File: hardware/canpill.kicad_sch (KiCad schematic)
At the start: 57 parts, among them J1 TYPE-C-31-M-12, J2 5100TR, J3 5100TR, J4 1776112-4, J5 Conn_01x20_Pin, J6 Conn_01x16_Pin, J7 FTSH-105-01-L-DV-K, SW1 SW_SPDT, SW2 SW_Push, U1 STM32F103C8T6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

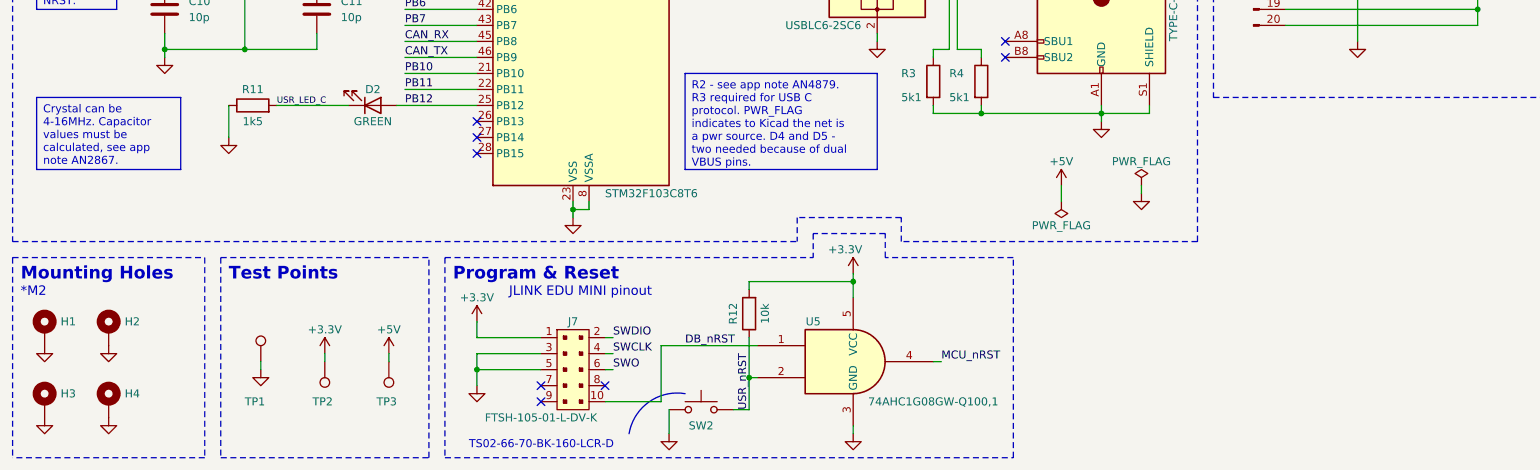
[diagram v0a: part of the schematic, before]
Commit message: (software:canpill_test) initial commit; (hardware) add pull-up on DB_nRST
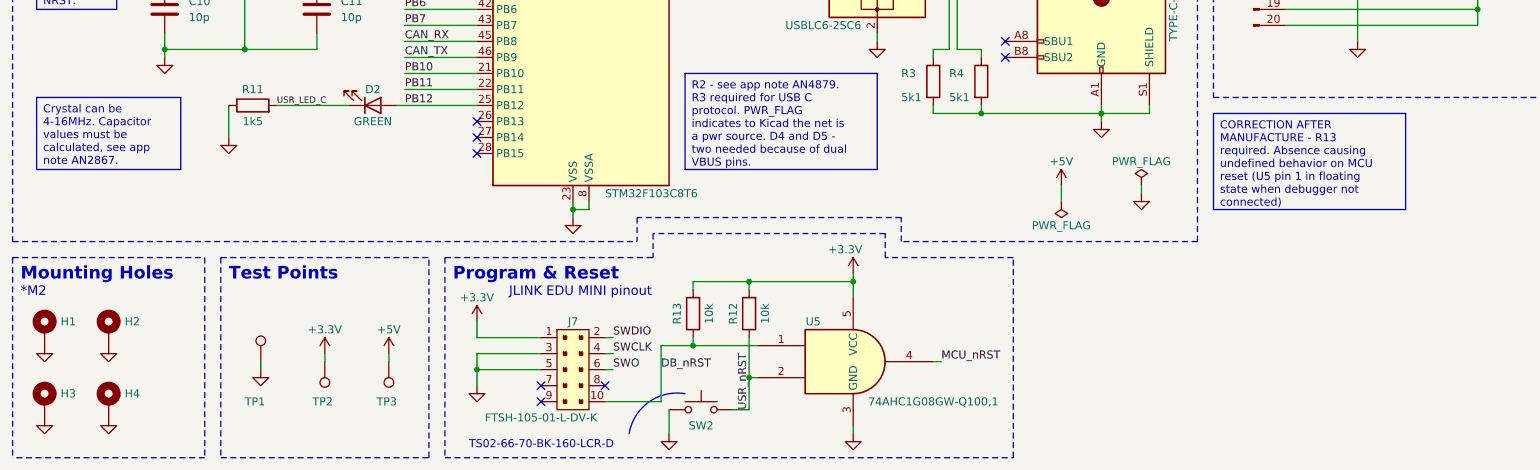
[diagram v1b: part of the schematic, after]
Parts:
- added R13: 10k, Resistor_SMD:R_0402_1005Metric, symbol Device:R
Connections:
- net +3.3V: now also R13.2
- net DB_nRST: now also R13.1
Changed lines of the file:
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@@
   (junction (at 148.59 167.64) (diameter 0) (color 0 0 0 0)
   )
+  (junction (at 123.19 177.8) (diameter 0) (color 0 0 0 0)
+  )
   (junction (at 182.88 24.13) (diameter 0) (color 0 0 0 0)
   )
@@
   )
   (junction (at 228.6 81.28) (diameter 0) (color 0 0 0 0)
+  )
+  (junction (at 132.08 167.64) (diameter 0) (color 0 0 0 0)
   )
   (junction (at 254 119.38) (diameter 0) (color 0 0 0 0)
@@
     (stroke (width 0) (type default))
   )
-  (wire (pts (xy 118.11 177.8) (xy 133.35 177.8))
-    (stroke (width 0) (type default))
-  )
   (wire (pts (xy 77.47 134.62) (xy 88.9 134.62))
     (stroke (width 0) (type default))
@@
     (stroke (width 0) (type dash))
   )
-  (polyline (pts (xy 15.24 161.29) (xy 139.7 161.29))
+  (polyline (pts (xy 15.24 161.29) (xy 114.3 161.29))
     (stroke (width 0) (type dash))
   )
@@
     (stroke (width 0) (type default))
   )
+  (wire (pts (xy 123.19 168.91) (xy 123.19 167.64))
+    (stroke (width 0) (type default))
+  )
   (polyline (pts (xy 15.24 15.24) (xy 107.95 15.24))
     (stroke (width 0) (type dash))
@@
     (stroke (width 0) (type default))
   )
+  (wire (pts (xy 123.19 177.8) (xy 133.35 177.8))
+    (stroke (width 0) (type default))
+  )
   (wire (pts (xy 63.5 90.17) (xy 64.77 90.17))
     (stroke (width 0) (type default))
@@
     (stroke (width 0) (type default))
   )
-  (polyline (pts (xy 139.7 157.48) (xy 139.7 161.29))
+  (polyline (pts (xy 114.3 157.48) (xy 114.3 161.29))
     (stroke (width 0) (type dash))
   )
@@
     (stroke (width 0) (type default))
   )
-  (polyline (pts (xy 156.21 157.48) (xy 139.7 157.48))
+  (polyline (pts (xy 156.21 157.48) (xy 114.3 157.48))
     (stroke (width 0) (type dash))
   )
@@
     (stroke (width 0) (type default))
   )
-  (polyline (pts (xy 142.24 160.02) (xy 142.24 163.83))
+  (polyline (pts (xy 116.84 160.02) (xy 116.84 163.83))
     (stroke (width 0) (type dash))
   )
@@
     (stroke (width 0) (type default))
   )
+  (wire (pts (xy 118.11 177.8) (xy 123.19 177.8))
+    (stroke (width 0) (type default))
+  )
   (wire (pts (xy 20.32 35.56) (xy 20.32 33.02))
     (stroke (width 0) (type default))
@@
     (stroke (width 0) (type default))
   )
-  (polyline (pts (xy 153.67 160.02) (xy 142.24 160.02))
+  (polyline (pts (xy 153.67 160.02) (xy 116.84 160.02))
     (stroke (width 0) (type dash))
   )
@@
     (stroke (width 0) (type default))
   )
+  (wire (pts (xy 123.19 176.53) (xy 123.19 177.8))
+    (stroke (width 0) (type default))
+  )
   (wire (pts (xy 238.76 116.84) (xy 242.57 116.84))
     (stroke (width 0) (type default))
@@
     (stroke (width 0) (type default))
   )
+  (wire (pts (xy 123.19 167.64) (xy 132.08 167.64))
+    (stroke (width 0) (type default))
+  )
   (wire (pts (xy 132.08 182.88) (xy 133.35 182.88))
     (stroke (width 0) (type default))
@@
     (stroke (width 0) (type default))
   )
-  (polyline (pts (xy 83.82 163.83) (xy 142.24 163.83))
+  (polyline (pts (xy 83.82 163.83) (xy 116.84 163.83))
     (stroke (width 0) (type dash))
   )
@@
     (effects (font (size 1.27 1.27)) (justify left top))
   )
+  (text_box "CORRECTION AFTER MANUFACTURE - R13 required. Absence causing undefined behavior on MCU reset (U5 pin 1 in floating state when debugger not connected)"
+    (at 205.74 140.97 0) (size 30.48 15.24)
+    (stroke (width 0) (type default))
+    (fill (type color) (color 0 0 0 0))
+    (effects (font (size 1.27 1.27)) (justify left top))
+  )
   (text_box "R2 - see app note AN4879. R3 required for USB C protocol. PWR_FLAG indicates to Kicad the net is a pwr source. D4 and D5 - two needed because of dual VBUS pins."
     (at 121.92 134.62 0) (size 30.48 15.24)
@@
     (effects (font (size 1.27 1.27)) (justify left bottom))
   )
-  (label "DB_nRST" (at 121.92 177.8 0) (fields_autoplaced)
-    (effects (font (size 1.27 1.27)) (justify left bottom))
-  )
   (label "SWCLK" (at 123.19 116.84 0) (fields_autoplaced)
     (effects (font (size 1.27 1.27)) (justify left bottom))
@@
   )
   (label "RS" (at 158.75 40.64 0) (fields_autoplaced)
+    (effects (font (size 1.27 1.27)) (justify left bottom))
+  )
+  (label "DB_nRST" (at 118.11 181.61 0) (fields_autoplaced)
     (effects (font (size 1.27 1.27)) (justify left bottom))
   )
@@
         )
       )
+    )
+  )
+  (symbol (lib_id "Device:R") (at 123.19 172.72 180) (unit 1)
+    (in_bom yes) (on_board yes) (dnp no)
+    (property "Reference" "R13" (at 120.65 172.72 90)
+      (effects (font (size 1.27 1.27)))
+    )
+    (property "Value" "10k" (at 125.73 172.72 90)
+      (effects (font (size 1.27 1.27)))
+    )
+    (property "Footprint" "Resistor_SMD:R_0402_1005Metric" (at 124.968 172.72 90)
+      (effects (font (size 1.27 1.27)) hide)
+    )
+    (property "Datasheet" "~" (at 123.19 172.72 0)
+      (effects (font (size 1.27 1.27)) hide)
+    )
+    (pin "1")
+    (pin "2")
+    (instances
+      (project "canpill"
+        (path "/5e2f4299-ac0c-4237-81d7-3a80b30bbe6f"
+          (reference "R13") (unit 1)
+        )
+      )
